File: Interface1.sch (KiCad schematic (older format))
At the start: 38 parts, among them J3 43045-0401, J4 43045-0401, J5 B2B-ZR, J6 B2B-ZR, Q7 BSS138W, SW1 TVBP06, SW2 TVBP06, U11 ATA6561-GAQW-N, U12 TXS0102DCUR

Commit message: PVT
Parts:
- removed C69: 100n, Capacitor-Chip:C_CHIP_1005_Hand_NoSilk, symbol passive:C
- removed C70, C71: 1u, Capacitor-Chip:C_CHIP_1005_Hand_NoSilk, symbol passive:C
- removed C73: 100p, Capacitor-Chip:C_CHIP_1005_Hand_NoSilk, symbol passive:C
- removed J6: B2B-ZR, Connector-JST:B2B-ZR, symbol Connector_Generic:Conn_01x02
- removed R45, R46: DNP(0), Resistor-Chip:R_CHIP_1005_Hand_NoSilk, symbol passive:R
- removed R47, R49: 1k, Resistor-Chip:R_CHIP_1005_Hand_NoSilk, symbol passive:R
- removed R48, R50: 62, Resistor-Chip:R_CHIP_2012_Reflow, symbol passive:R
- removed TP24: CANTX, Print:TP_C0.8, symbol print:TestPoint
- removed TP25: CANRX, Print:TP_C0.8, symbol print:TestPoint
- removed U11: ATA6561-GAQW-N, IC-SOP:SOP8-W3.9, symbol interface-microchip:ATA6561-GAQW
- removed U12: TXS0102DCUR, IC-SOP:VSSOP8, symbol interface-ti:TXS0102DCU
- added J3: B2B-ZR, Connector-JST:B2B-ZR, symbol Connector_Generic:Conn_01x02
- SW1: value TVBP06 -> TVBP06-B043CU-B; PartName TVBP06 -> TVBP06-B043CU-B
- SW2: value TVBP06 -> TVBP06-B043CW-B; PartName TVBP06 -> TVBP06-B043CW-B
- renumbered C72 to C69, C74 to C70, C75 to C71, J3 to J4, J4 to J5, J5 to J6, R51 to R44, R52 to R45, R53 to R46, R54 to R47, R55 to R48, R56 to R49, R57 to R50
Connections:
- net +5V: now also J3.1 (Pin_1); no longer R45.1
- net GND: now also J3.2 (Pin_2)
- net KICKER_CAN+ renamed KICKER_P
- net KICKER_CAN- renamed KICKER_N
- new net USB5V: R45.1
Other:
- note added: "Fan"
- note removed: "Use CAN -> pull-down\nUse UART -> pull-up"
- moved on the sheet: C69, C70, C71, D10, D11, D12, D13, D14, D8, D9, J4, J5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

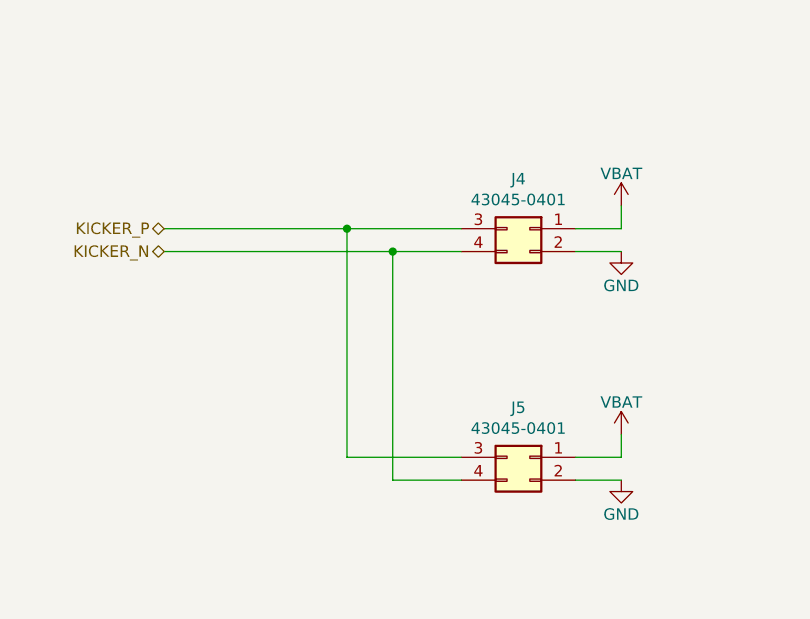
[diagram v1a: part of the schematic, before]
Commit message: SBUにTVSダイオードを追加
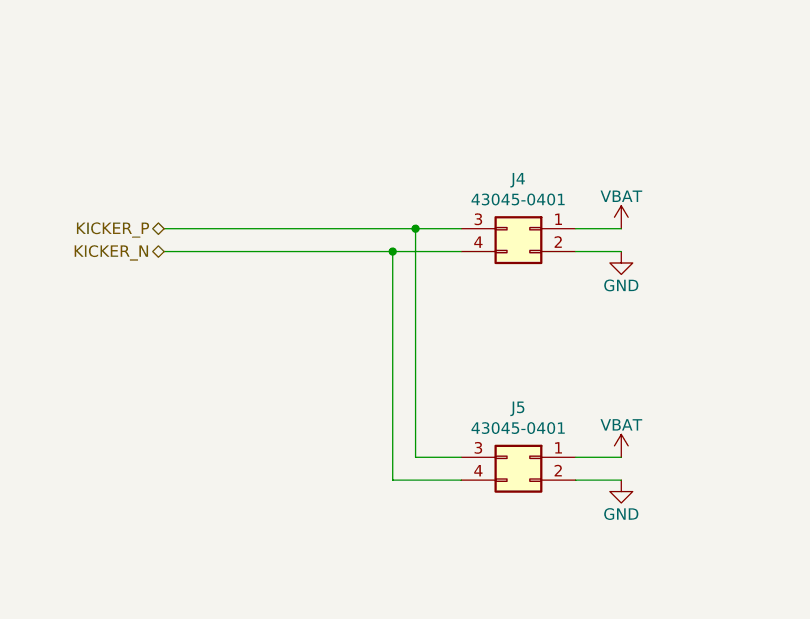
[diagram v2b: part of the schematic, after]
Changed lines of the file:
@@
 L supply-alias:VBAT #PWR0142
 U 1 1 5EA7C2F7
-P 3500 1900
-F 0 "#PWR0142" H 3500 1750 50  0001 C CNN
-F 1 "VBAT" H 3500 2040 50  0000 C CNN
-F 2 "" H 3500 1900 50  0001 C CNN
-F 3 "" H 3500 1900 50  0001 C CNN
-	1    3500 1900
+P 3500 2000
+F 0 "#PWR0142" H 3500 1850 50  0001 C CNN
+F 1 "VBAT" H 3500 2140 50  0000 C CNN
+F 2 "" H 3500 2000 50  0001 C CNN
+F 3 "" H 3500 2000 50  0001 C CNN
+	1    3500 2000
 	1    0    0    -1
 $EndComp
@@
 L supply-alias:VBAT #PWR0144
 U 1 1 5FB780A7
-P 3500 2900
-F 0 "#PWR0144" H 3500 2750 50  0001 C CNN
-F 1 "VBAT" H 3500 3040 50  0000 C CNN
-F 2 "" H 3500 2900 50  0001 C CNN
-F 3 "" H 3500 2900 50  0001 C CNN
-	1    3500 2900
+P 3500 3000
+F 0 "#PWR0144" H 3500 2850 50  0001 C CNN
+F 1 "VBAT" H 3500 3140 50  0000 C CNN
+F 2 "" H 3500 3000 50  0001 C CNN
+F 3 "" H 3500 3000 50  0001 C CNN
+	1    3500 3000
 	1    0    0    -1
 $EndComp
@@
 Wire Wire Line
 	3300 3100 3500 3100
-Wire Wire Line
-	3500 1900 3500 2000
-Wire Wire Line
-	3500 2900 3500 3000
 $Comp
 L diode:D_LED D8
@@
 	2800 3100 2500 3100
 Wire Wire Line
-	2300 3000 2800 3000
+	2600 3000 2800 3000
 Wire Wire Line
 	2500 2100 2500 3100
 Wire Wire Line
-	2300 2000 2300 3000
+	2600 2000 2600 3000
 Wire Wire Line
 	2800 2100 2500 2100
 Wire Wire Line
-	2300 2000 2800 2000
+	2600 2000 2800 2000
 Connection ~ 2500 2100
-Connection ~ 2300 2000
+Connection ~ 2600 2000
 $Comp
 L passive:C C70
@@
 	7000 2600 7000 2800
 Wire Wire Line
-	1500 2000 2300 2000
+	1500 2000 2600 2000
 Wire Wire Line
 	1500 2100 2500 2100
